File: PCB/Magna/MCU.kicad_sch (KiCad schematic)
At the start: 54 parts, among them J201 Conn_02x06_Odd_Even, J202 Conn_ARM_JTAG_SWD_20, J203 Boot Jumper, U201 STM32F730V8T6, U202 24.576 MHz, Y201 25MHz

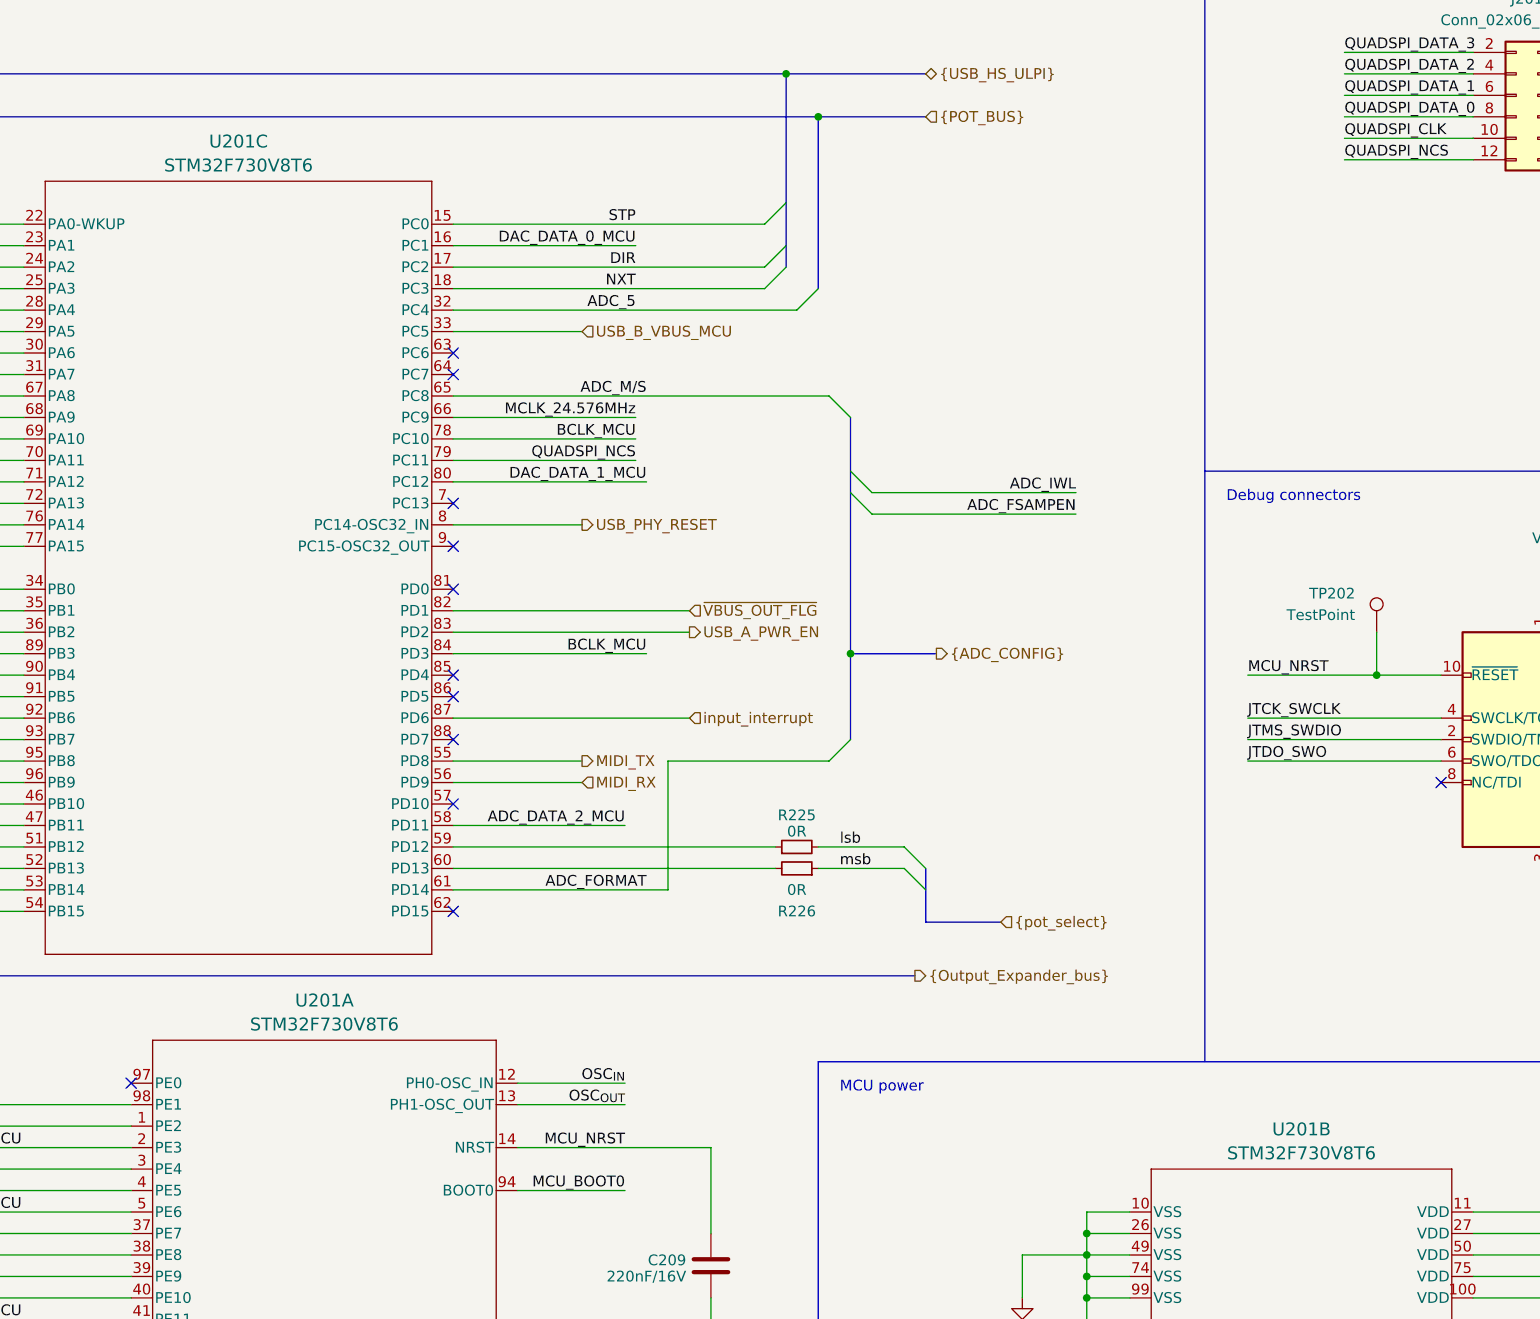
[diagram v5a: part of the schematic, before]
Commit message: Commit with small changes for production
Mainboard and IO board was manufactored with this version
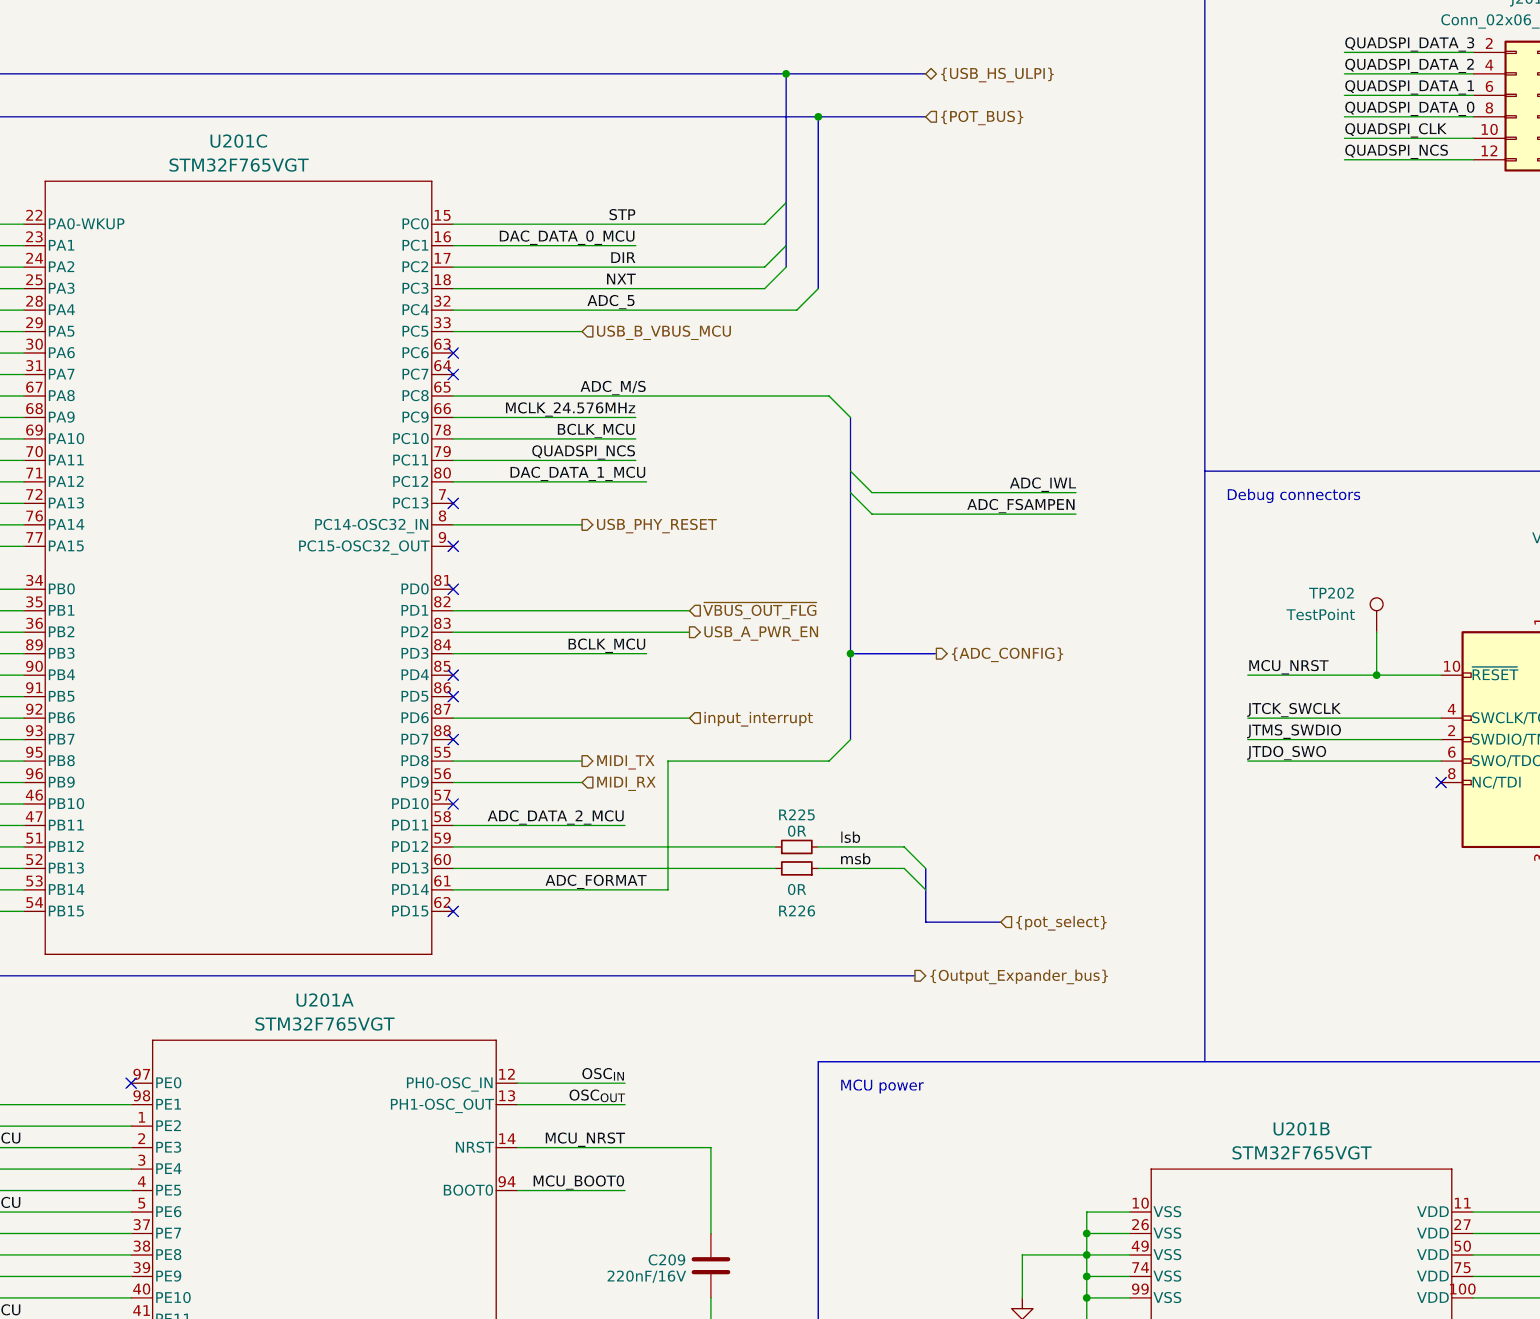
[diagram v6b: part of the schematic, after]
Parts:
- U201: value STM32F730V8T6 -> STM32F765VGT; LCSC C404010 -> C435845
- U202: LCSC C387393 -> C5203547
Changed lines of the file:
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@@
 			)
 		)
-		(property "Value" "STM32F730V8T6"
+		(property "Value" "STM32F765VGT"
 			(at 106.68 59.099 0)
 			(effects
@@
 			)
 		)
-		(property "Datasheet" "STM32H750VBT6"
+		(property "Datasheet" "https://www.st.com/resource/en/datasheet/stm32f765vg.pdf"
 			(at 76.2 66.04 0)
 			(effects
@@
 			)
 		)
-		(property "LCSC" "C404010"
+		(property "LCSC" "C435845"
 			(at 76.2 66.04 0)
 			(effects
@@
 			)
 		)
-		(property "Value" "STM32F730V8T6"
+		(property "Value" "STM32F765VGT"
 			(at 232.41 175.939 0)
 			(effects
@@
 			)
 		)
-		(property "Datasheet" "STM32H750VBT6"
+		(property "Datasheet" "https://www.st.com/resource/en/datasheet/stm32f765vg.pdf"
 			(at 207.01 182.88 0)
 			(effects
@@
 			)
 		)
-		(property "LCSC" "C404010"
+		(property "LCSC" "C435845"
 			(at 207.01 182.88 0)
 			(effects
@@
 			)
 		)
-		(property "LCSC" "C387393"
+		(property "LCSC" "C5203547"
 			(at 345.44 99.06 0)
 			(effects
@@
 			)
 		)
-		(property "Value" "STM32F730V8T6"
+		(property "Value" "STM32F765VGT"
 			(at 116.84 160.699 0)
 			(effects
@@
 			)
 		)
-		(property "Datasheet" "STM32H750VBT6"
+		(property "Datasheet" "https://www.st.com/resource/en/datasheet/stm32f765vg.pdf"
 			(at 88.9 167.64 0)
 			(effects
@@
 			)
 		)
-		(property "LCSC" "C404010"
+		(property "LCSC" "C435845"
 			(at 88.9 167.64 0)
 			(effects

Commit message: Update incorrect footprints on mainboard
For some reason footprints were incorrect on midi part.
Also 24.576MHz oscillator was incorrect.
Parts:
- U202: footprint Oscillator:Oscillator_SMD_ECS_2520MV-xxx-xx-4Pin_2.5x2.0mm -> Crystal:Crystal_SMD_3225-4Pin_3.2x2.5mm_HandSoldering
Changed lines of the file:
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@@
 			)
 		)
-		(property "Footprint" "Oscillator:Oscillator_SMD_ECS_2520MV-xxx-xx-4Pin_2.5x2.0mm"
+		(property "Footprint" "Crystal:Crystal_SMD_3225-4Pin_3.2x2.5mm_HandSoldering"
 			(at 356.87 107.95 0)
 			(effects

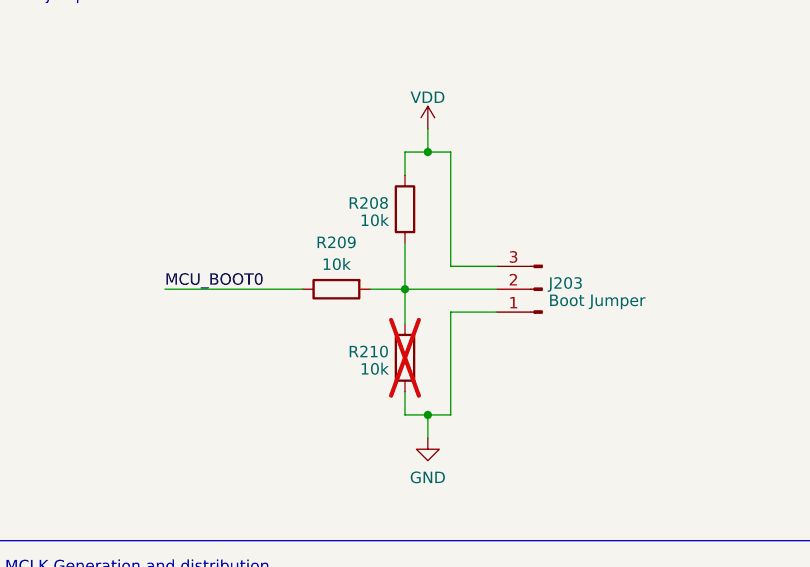
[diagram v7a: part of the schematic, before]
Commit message: Fix stack size and memory placements
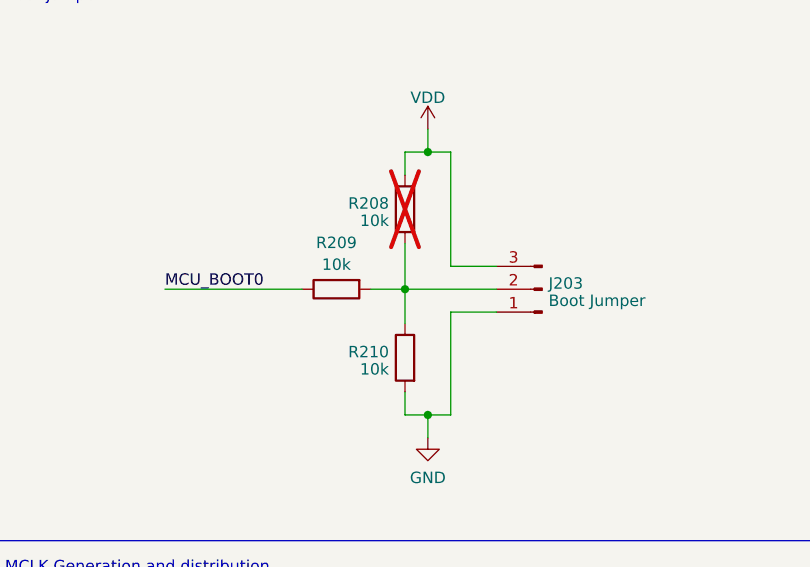
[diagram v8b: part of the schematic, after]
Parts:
- R208: now not fitted; now left out of the parts list
- R210: now fitted; now in the parts list
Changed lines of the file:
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@@
 		(unit 1)
 		(exclude_from_sim no)
-		(in_bom yes)
+		(in_bom no)
 		(on_board yes)
-		(dnp no)
+		(dnp yes)
 		(property "Reference" "R208"
 			(at 344.932 37.4563 0)
@@
 		(unit 1)
 		(exclude_from_sim no)
-		(in_bom no)
+		(in_bom yes)
 		(on_board yes)
-		(dnp yes)
+		(dnp no)
 		(property "Reference" "R210"
 			(at 344.932 53.9663 0)
